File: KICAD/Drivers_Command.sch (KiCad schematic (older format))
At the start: 14 parts, among them U4 CD4053BM96, U5 CD4053BM96, U6 4011

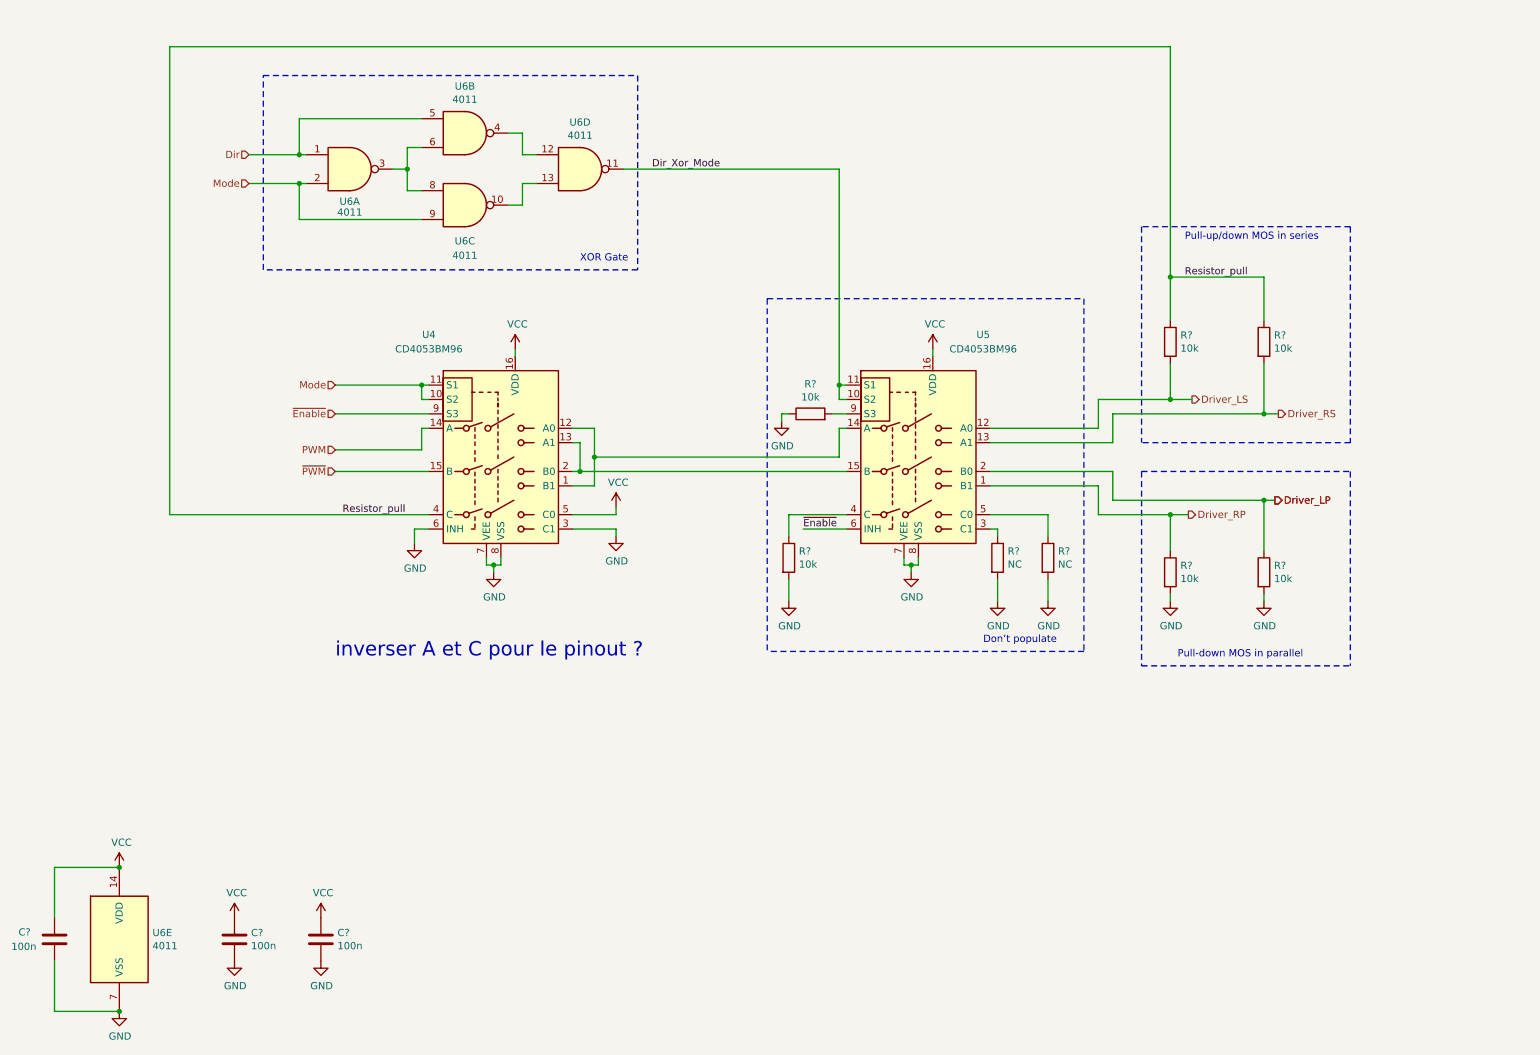
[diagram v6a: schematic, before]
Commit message: drivers draft + clean and minors changes
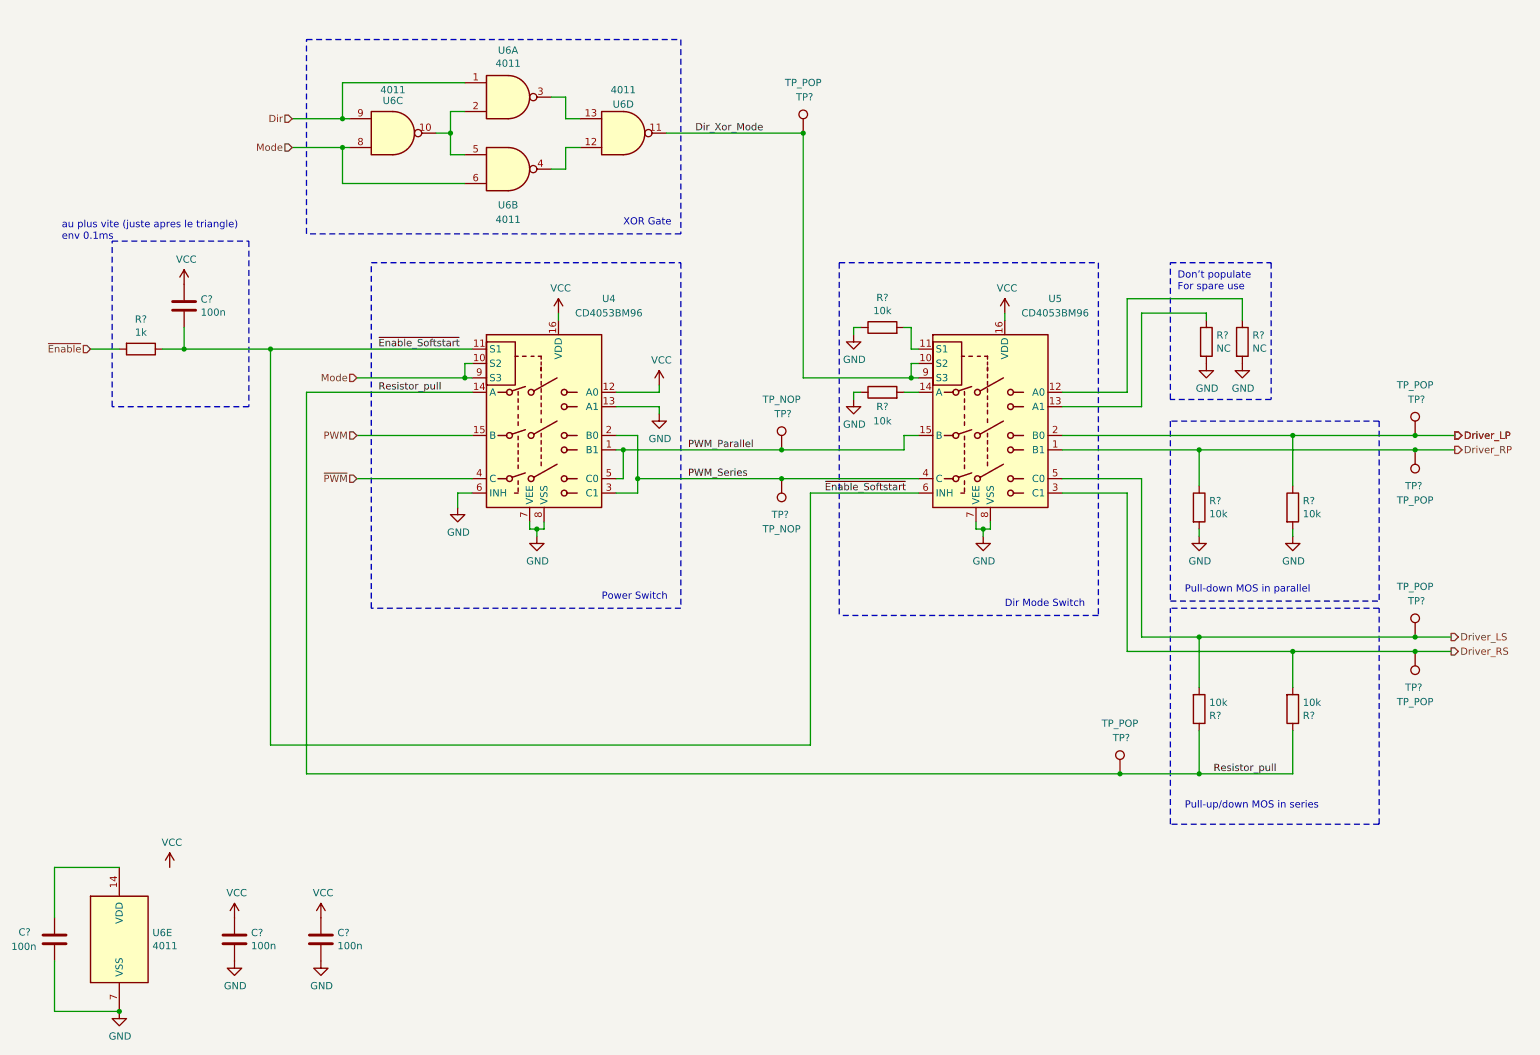
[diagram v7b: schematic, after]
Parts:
- removed R?: NC, Resistor_SMD:R_0805_2012Metric_Pad1.15x1.40mm_HandSolder, symbol Device:R
- removed R?: 10k, Resistor_SMD:R_0805_2012Metric_Pad1.15x1.40mm_HandSolder, symbol Device:R
- added C?: 100n, symbol Device:C
- added R?: 10k, Resistor_SMD:R_0805_2012Metric_Pad1.15x1.40mm_HandSolder, symbol Device:R
- added R?: NC, Resistor_SMD:R_0805_2012Metric_Pad1.15x1.40mm_HandSolder, symbol Device:R
- added R?: 1k, Resistor_SMD:R_0805_2012Metric_Pad1.15x1.40mm_HandSolder, symbol Device:R
- added TP? (x6): TP_POP, symbol Connector:TestPoint
- added TP? (x2): TP_NOP, symbol Connector:TestPoint
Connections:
- net Dir: now also U6.1, U6.9; no longer U6.1, U6.5
- net Dir_Xor_Mode: now also U5.9 (S3), TP?.1; no longer U5.11 (S1)
- net Driver_LP: now also TP?.1
- net Driver_LS: now also U5.5 (C0), TP?.1; no longer U5.12 (A0)
- net Driver_RP: now also TP?.1
- net Driver_RS: now also U5.3 (C1), TP?.1; no longer U5.13 (A1)
- net GND: now also U4.13 (A1), R?.1, R?.2; no longer U4.3 (C1)
- net Mode: now also U4.9 (S3), U6.6, U6.8; no longer U4.11 (S1), U6.2, U6.9
- net PWM: now also U4.15 (B); no longer U4.14 (A)
- net Resistor_pull: now also U4.14 (A), TP?.1; no longer U4.4 (C)
- net VCC: now also U4.12 (A0), C?.1; no longer C?.1, U4.5 (C0), U6.14 (VDD)
- net ~Enable: now also R?.2; no longer U4.9 (S3), U5.6 (INH)
- net ~PWM: now also U4.4 (C); no longer U4.15 (B)
- net at R?.1: now also U5.13 (A1); no longer U5.3 (C1)
- net PWM_Series: now reaches U5.4 (C)
- net PWM_Series: now also U4.2 (B0), U4.3 (C1), TP?.1
- net at R?.2: now also U5.11 (S1); no longer U5.9 (S3)
- net at U6.13: now also U6.3; no longer U6.10
- net at U6.12: now also U6.4; no longer U6.4
- new net: C?.1, U6.14 (VDD)
- new net: R?.1, U5.12 (A0)
- new net: R?.2, U5.14 (A)
- new net: U6.10, U6.2, U6.5
- new net PWM_Parallel: TP?.1, U4.1 (B1), U4.5 (C0), U5.15 (B)
- new net ~Enable_Softstart: C?.2, R?.1, U4.11 (S1), U5.6 (INH)
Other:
- note added: "Dir Mode Switch"
- note added: "Don’t populate\nFor spare use"
- note added: "Power Switch"
- note added: "au plus vite (juste apres le triangle)\nenv 0.1ms"
- note removed: "Don’t populate"
- note removed: "inverser A et C pour le pinout ?"
- moved on the sheet: R?, U4, U5, U6D

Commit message: driver + clean clean clean
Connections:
- net VCC: now also C?.1, U6.14 (VDD)
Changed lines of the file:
@@
 $Descr A4 11693 8268
 encoding utf-8
-Sheet 5 16
+Sheet 5 17
 Title "SESAME"
 Date "2021-08-04"
@@
 L power:VCC #PWR0175
 U 1 1 615841AD
-P 1650 6500
-F 0 "#PWR0175" H 1650 6350 50  0001 C CNN
-F 1 "VCC" H 1665 6673 50  0000 C CNN
-F 2 "" H 1650 6500 50  0001 C CNN
-F 3 "" H 1650 6500 50  0001 C CNN
-	1    1650 6500
+P 1300 6500
+F 0 "#PWR0175" H 1300 6350 50  0001 C CNN
+F 1 "VCC" H 1315 6673 50  0000 C CNN
+F 2 "" H 1300 6500 50  0001 C CNN
+F 3 "" H 1300 6500 50  0001 C CNN
+	1    1300 6500
 	1    0    0    -1
 $EndComp
@@
 Text HLabel 1100 2900 0    50   Input ~ 0
 ~Enable
+Connection ~ 1300 6500
 $EndSCHEMATC
